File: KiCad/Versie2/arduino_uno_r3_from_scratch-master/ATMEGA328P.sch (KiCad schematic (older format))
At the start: 12 parts, among them SW1 RESET_SWITCH, U5 ATMEGA328P, X2 CSTCE16MOV53-R0

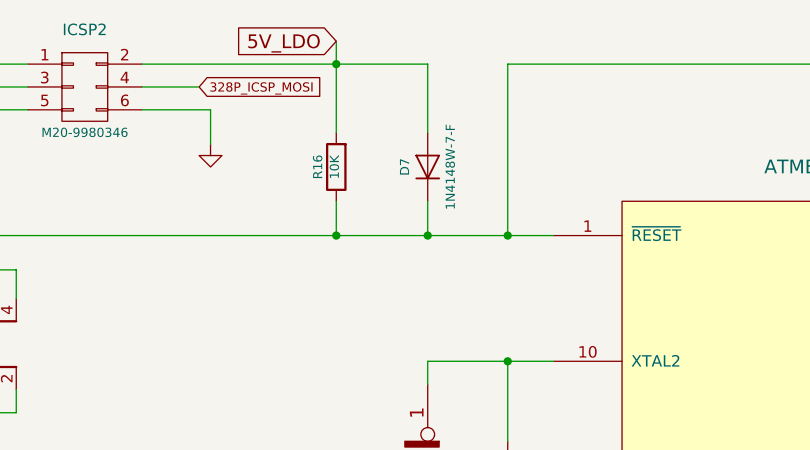
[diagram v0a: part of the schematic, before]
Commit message: 28feb
Aanpassing KiCad+deel footprints
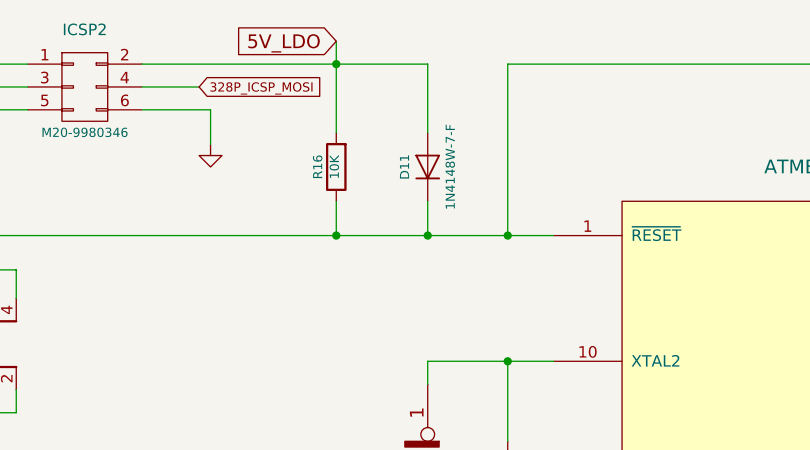
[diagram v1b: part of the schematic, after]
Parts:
- renumbered D7 to D11
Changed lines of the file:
@@
 $EndComp
 $Comp
-L D D7
+L D D11
 U 1 1 55E8CABC
 P 5300 1200
-F 0 "D7" H 5300 1300 40  0000 C CNN
+F 0 "D11" H 5300 1300 40  0000 C CNN
 F 1 "1N4148W-7-F" H 5300 1100 40  0000 C CNN
 F 2 "~" H 5300 1200 60  0000 C CNN
